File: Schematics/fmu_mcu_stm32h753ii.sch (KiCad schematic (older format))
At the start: 20 parts, among them U1 STM32H753IIKx

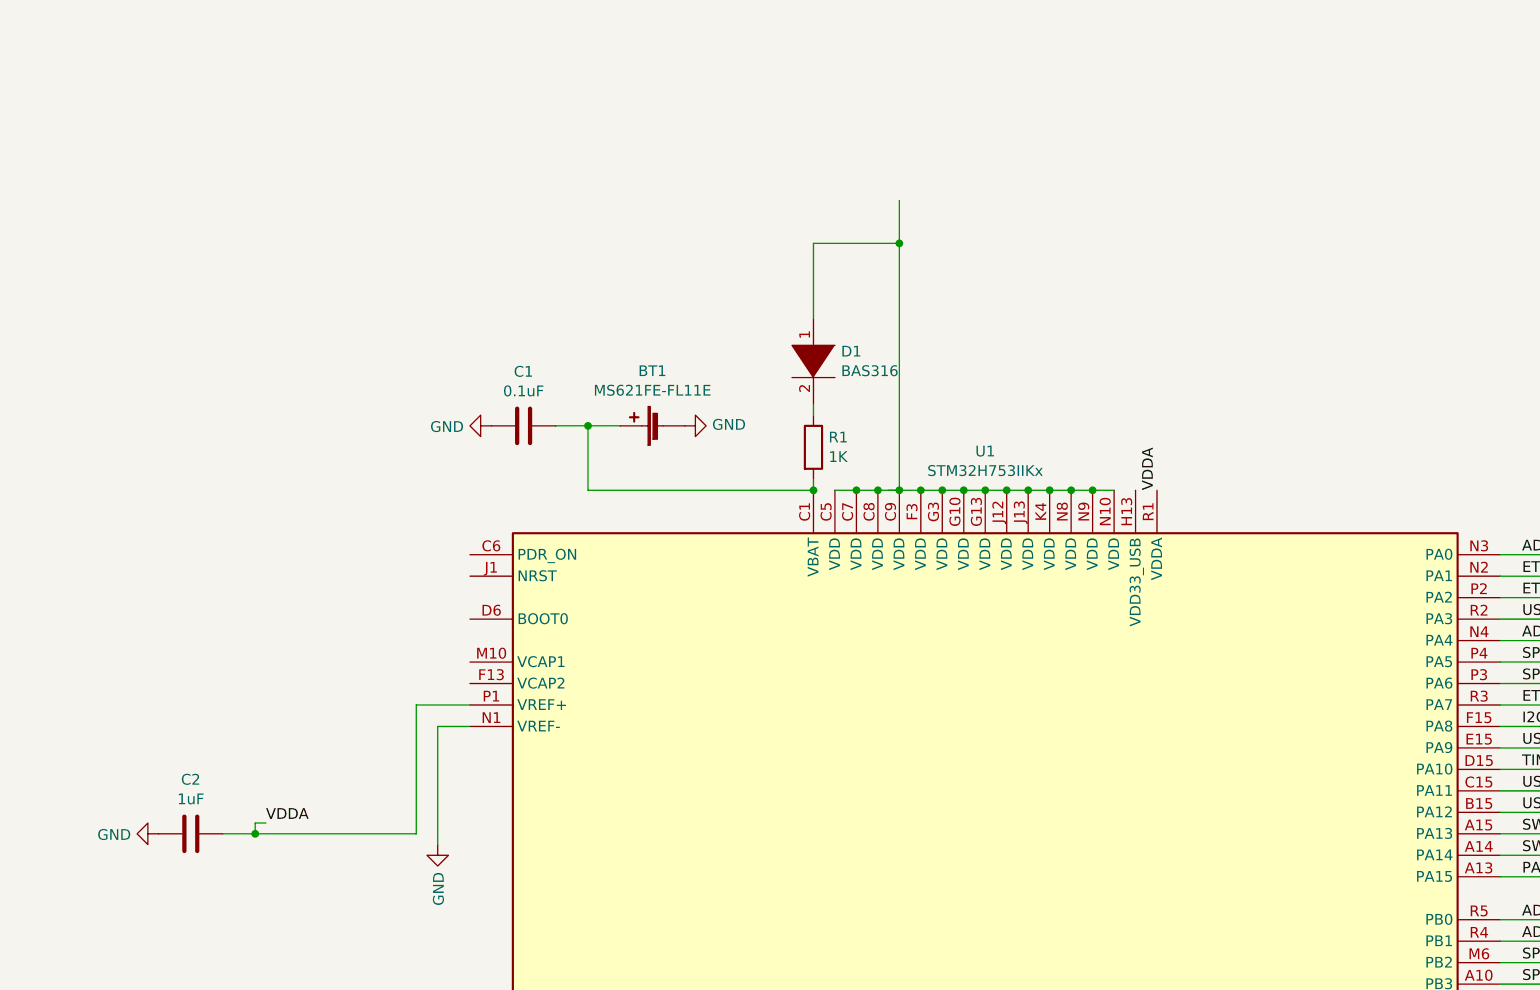
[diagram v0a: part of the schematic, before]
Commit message: add reference docs, rearrange schematics
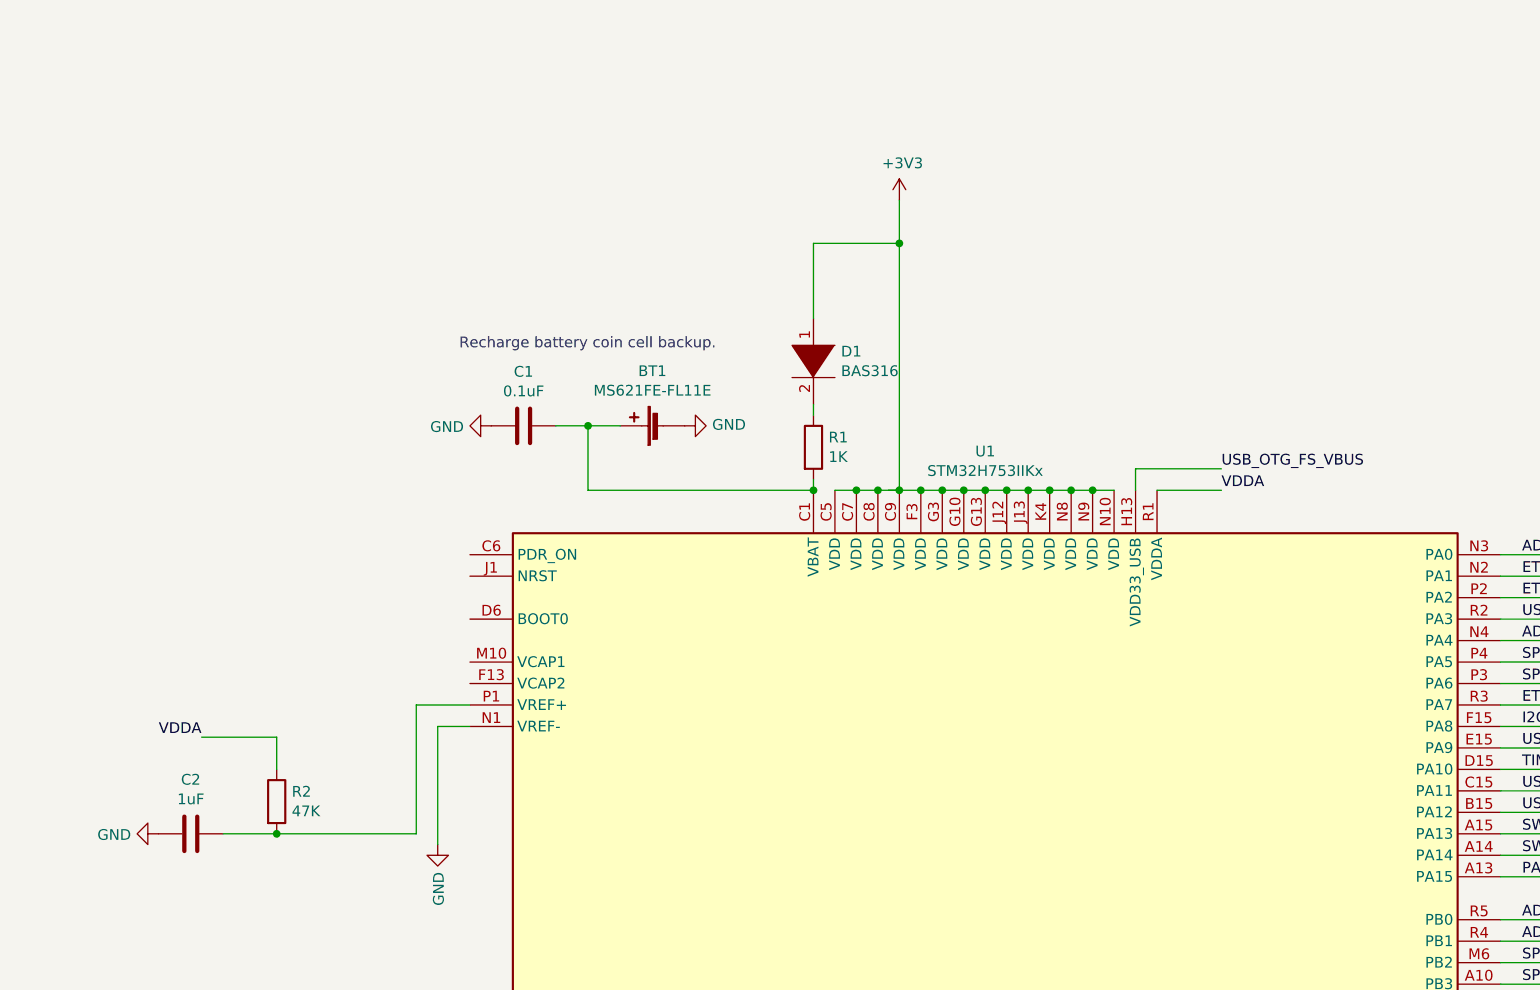
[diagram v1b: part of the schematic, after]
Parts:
- added R2: 47K, symbol Device:R
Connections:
- net +3V3: now also D1.1 (K), U1.C5 (VDD), U1.C7 (VDD), U1.C8 (VDD), U1.C9 (VDD), U1.F3 (VDD), U1.G10 (VDD), U1.G13 (VDD), U1.G3 (VDD), U1.J12 (VDD), U1.J13 (VDD), U1.K4 (VDD), U1.N10 (VDD), U1.N8 (VDD), U1.N9 (VDD)
- net VBUS: now also U1.H13 (VDD33_USB)
- net VDDA: now also R2.1; no longer C2.2, U1.P1 (VREF+)
- new net: C2.2, R2.2, U1.P1 (VREF+)
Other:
- note added: "Recharge battery coin cell backup."
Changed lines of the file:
@@
 	6300 2750 6150 2750
 Connection ~ 6150 2750
-Text Label 8800 3050 1    50   ~ 0
-VDDA
 $Comp
 L power:+3V3 #PWR?
@@
 Wire Wire Line
 	5450 4150 5600 4150
-Wire Wire Line
-	4600 4650 4450 4650
-Wire Wire Line
-	4600 4600 4600 4650
-Wire Wire Line
-	4650 4600 4600 4600
-Text Label 4650 4600 0    50   ~ 0
-VDDA
 $Comp
 L power:GND #PWR?
@@
 $EndComp
 Wire Wire Line
-	4600 4650 5350 4650
-Wire Wire Line
 	5350 4650 5350 4050
 Wire Wire Line
 	5350 4050 5600 4050
-Connection ~ 4600 4650
 Wire Wire Line
 	7550 3050 7600 3050
@@
 Wire Notes Line
 	15500 2400 21500 2400
+Text Notes 5550 2400 0    50   ~ 0
+Recharge battery coin cell backup.
+Wire Wire Line
+	8700 3050 8700 2950
+Wire Wire Line
+	8700 2950 9100 2950
+Text Label 9100 2950 0    50   ~ 0
+USB_OTG_FS_VBUS
+Wire Wire Line
+	8800 3050 9100 3050
+Text Label 9100 3050 0    50   ~ 0
+VDDA
+Wire Wire Line
+	4450 4650 4700 4650
+$Comp
+L Device:R R2
+U 1 1 6155D132
+P 4700 4500
+F 0 "R2" H 4770 4546 50  0000 L CNN
+F 1 "47K" H 4770 4455 50  0000 L CNN
+F 2 "" V 4630 4500 50  0001 C CNN
+F 3 "~" H 4700 4500 50  0001 C CNN
+	1    4700 4500
+	1    0    0    -1
+$EndComp
+Connection ~ 4700 4650
+Wire Wire Line
+	4700 4650 5350 4650
+Wire Wire Line
+	4700 4350 4700 4200
+Wire Wire Line
+	4700 4200 4350 4200
+Text Label 4350 4200 2    50   ~ 0
+VDDA
+$Comp
+L power:+3V3 #PWR?
+U 1 1 61582EE4
+P 7600 1700
+F 0 "#PWR?" H 7600 1550 50  0001 C CNN
+F 1 "+3V3" H 7615 1873 50  0000 C CNN
+F 2 "" H 7600 1700 50  0001 C CNN
+F 3 "" H 7600 1700 50  0001 C CNN
+	1    7600 1700
+	1    0    0    -1
+$EndComp
 $EndSCHEMATC

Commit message: upnext, power
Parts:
- added C17, C18: 2.2uF, symbol Device:C
- added JP1: TP29, symbol Jumper:Jumper_2_Bridged
- added R3: 2.2k, symbol Device:R
- added R4: 10K, symbol Device:R
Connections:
- net +3V3: now also U1.C6 (PDR_ON), JP1.2 (B), R4.1
- net GND: now also C17.2, C18.1, R3.2
- net at U1.D6 (BOOT0): now also JP1.1 (A), R3.1
- net at U1.F13 (VCAP2): now also C18.2
- net FMU_nRST: now reaches U1.J1 (NRST)
- net FMU_nRST: now also R4.2
- net at U1.M10 (VCAP1): now also C17.1
- net SPI1_MISO_SENSOR1_ICM20682 renamed SPI1_MISO_SENSOR1_ICM20602
- net UART4_RX_TELEM2 renamed UART5_RX_TELEM2
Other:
- moved on the sheet: C2, R2
